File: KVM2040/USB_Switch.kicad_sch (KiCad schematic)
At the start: 8 parts, among them J1 SS-52000-003, U1 TUSB8042AIRGCR, U2 SIT8008BC-71-18S-24.000000, U3 XTMUXHS4212RKSR, U4 PTMUXHS221NKGR

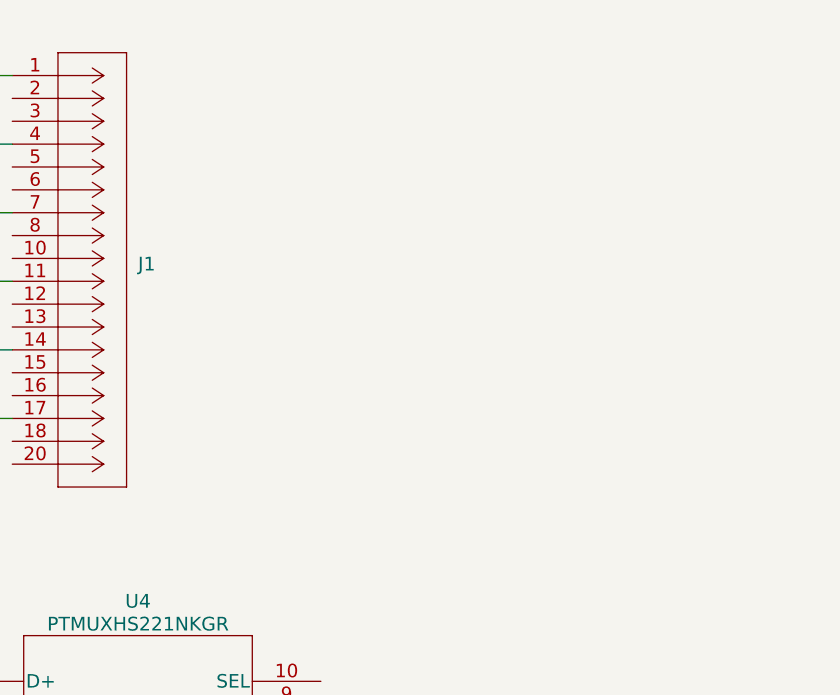
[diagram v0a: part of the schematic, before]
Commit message: USB-B replacement
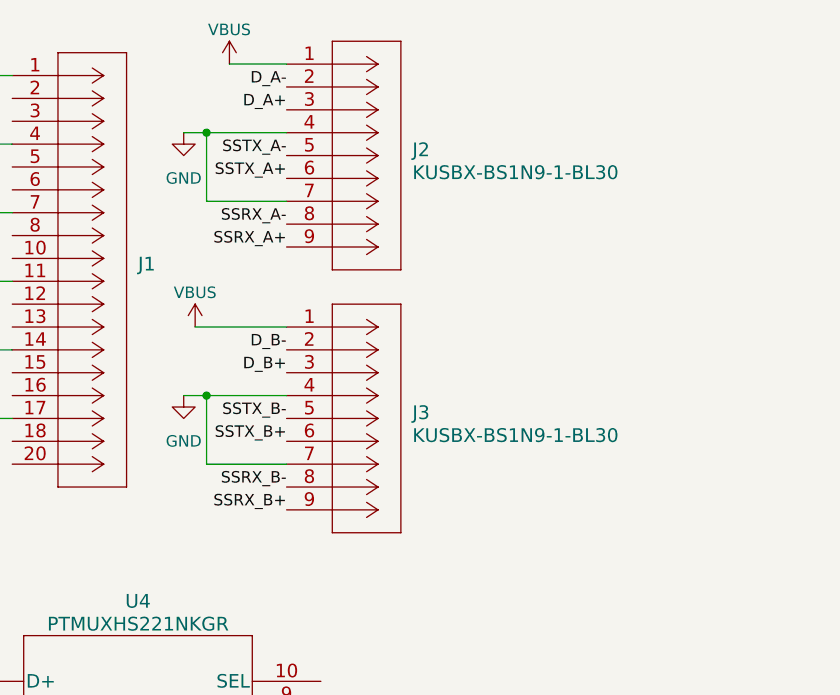
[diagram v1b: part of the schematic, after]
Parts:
- added J2, J3: KUSBX-BS1N9-1-BL30, KUSBX-BS1N9:KUSBX-BS1N9-1-BL30, symbol KUSBX-BS1N9:KUSBX-BS1N9-1-BL30
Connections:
- net D_A+: now also J2.3 (D+)
- net D_A-: now also J2.2 (D-)
- net D_B+: now also J3.3 (D+)
- net D_B-: now also J3.2 (D-)
- net GND: now also J2.4 (GND), J2.7 (GND-DRAIN), J3.4 (GND), J3.7 (GND-DRAIN)
- net SSRX_A+: now also J2.9 (STDB_SSRX+)
- net SSRX_A-: now also J2.8 (STDB_SSRX-)
- net SSRX_B+: now also J3.9 (STDB_SSRX+)
- net SSRX_B-: now also J3.8 (STDB_SSRX-)
- net SSTX_A+: now also J2.6 (STDB_SSTX+)
- net SSTX_A-: now also J2.5 (STDB_SSTX-)
- net SSTX_B+: now also J3.6 (STDB_SSTX+)
- net SSTX_B-: now also J3.5 (STDB_SSTX-)
- net VBUS: now also J2.1 (VBUS), J3.1 (VBUS)

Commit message: adding upstream port
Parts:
- added C3, C4: 0.1uF, Capacitor_SMD:C_0201_0603Metric, symbol Device:C
- added C5: 10uF, Capacitor_SMD:C_0402_1005Metric, symbol Device:C
- added R2, R3: 4.7k 5%, Resistor_SMD:R_0402_1005Metric, symbol Device:R
- added R4: 90.9K 1%, Resistor_SMD:R_0402_1005Metric, symbol Device:R
- added R5: 10k 1%, Resistor_SMD:R_0402_1005Metric, symbol Device:R
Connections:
- net +3.3V: now also U1.16 (VDD33)
- net D_C+: now also U1.53 (USB_DP_UP)
- net D_C-: now also U1.54 (USB_DM_UP)
- net GND: now also C5.2, R2.2, R3.2, R5.2
- net SSRX_C+: now also U1.58 (USB_SSRXP_UP)
- net SSTX_C+: now also C3.2
- net SSTX_C-: now also U1.59 (USB_SSRXM_UP), C4.2
- net VBUS: now also C5.1, R4.2; no longer U1.48 (USB_VBUS)
- net at U1.40 (FULLPWRMGMTz/SMBA1/SS_UP): now also R3.1
- net at U1.42 (GANGED/SMBA2/HS_UP): now also R2.1
- net at U1.55 (USB_SSTXP_UP): now also C3.1
- net at U1.56 (USB_SSTXM_UP): now also C4.1
- net IN_A_RX-: now reaches J1.10
- net IN_B_D+: now reaches J1.12
- net IN_B_D-: now reaches J1.13
- net IN_B_TX+: now reaches J1.15
- net IN_B_TX-: now reaches J1.16
- net IN_B_RX+: now reaches J1.18
- net IN_A_D+: now reaches J1.2
- net IN_B_RX-: now reaches J1.20
- net IN_A_D-: now reaches J1.3
- net IN_A_TX+: now reaches J1.5
- net IN_A_TX-: now reaches J1.6
- net IN_A_RX+: now reaches J1.8
- new net: R4.1, R5.1, U1.48 (USB_VBUS)
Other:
- moved on the sheet: U1
